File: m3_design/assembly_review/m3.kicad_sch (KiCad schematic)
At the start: 15 parts, among them J3 USB-C 2.0, U2 AP63203WU-7

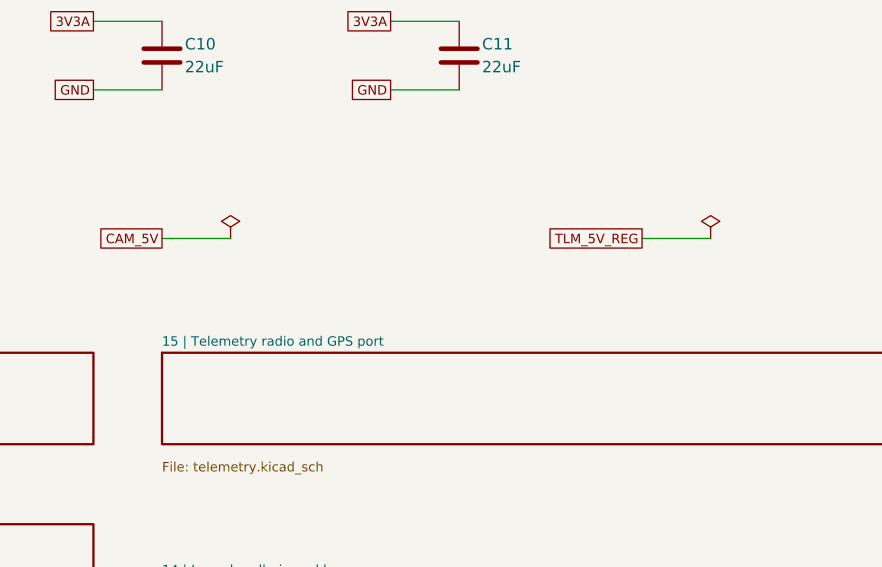
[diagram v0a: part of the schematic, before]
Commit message: M3-ASSY-R7: on-board GNSS and LoRa radio, clean-routing gate, owner-accepted deviations
R7 replaces R6's external radio/GPS harness ports with an on-board u-blox
MAX-F10S (U30, MAX-M10S drop-in) and EBYTE E22-900MM22S SX1262 radio (U31)
in an RF strip at the aft end, each with an edge-launch SMA jack (J30 GNSS,
J31 RADIO), RF ESD, an antenna-bias current limiter and DNP tuning pads.
The board grows to 46 x 118 mm (R6 copper translated +18 mm).

- Schematic, parts and footprints: r7_sch.py, r7_parts.py
- Reproducible board build from the SHA-checked R6 board: r7_build.sh
  (r7_pcb, r7_route, r7_redraw, r7_rework, r7_hygiene, r7_polish, r7_post)
- Gate: check_r7.py (RF contract), route_check.py (clean routing, M2)
  in tools/check.sh; fit_check, cost and procurement updated for R7
- Eight independent review passes with skeptic verification; pass 8 on
  this board found 0 Critical / 0 Major
- Owner accepted the deviation list on 2026-10-18 (R7_VALIDATION), with
  the 7.7 A servo-feed copper rise accepted as estimated

Board SHA-256 c872a3d30509cccf5f78b64cde48ef722ee85c7be23c4848b07ce4082a852de3.
tools/check.sh: DRC 0, unconnected 0, parity 0, ERC 0; audit, silk,
R7 contract, routing hygiene (0 failing), actuator contract and fit OK.
Before ordering: consign U4 and get JLC's forward-rail confirmation.

Co-Authored-By: Claude Opus 5.5 <noreply@anthropic.com>
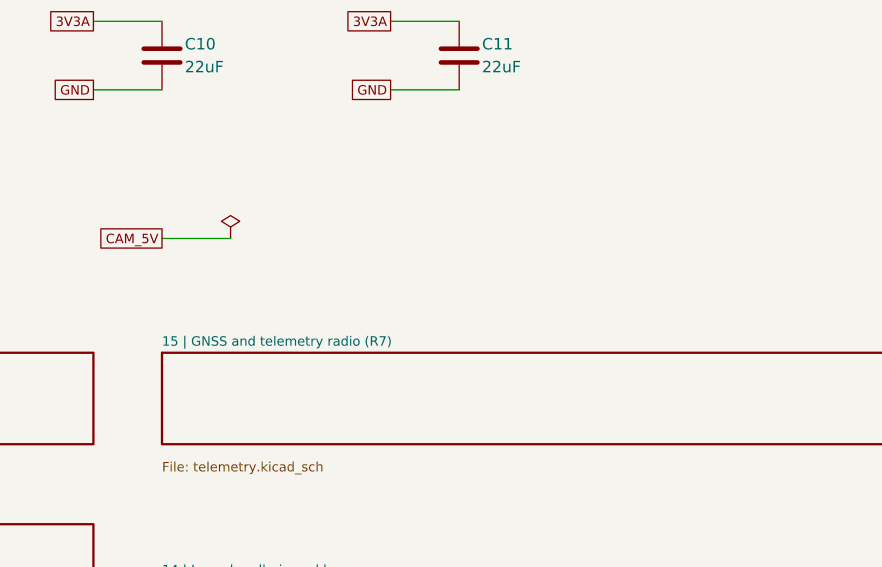
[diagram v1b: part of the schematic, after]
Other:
- sheet 15 | Telemetry radio and GPS port renamed 15 | GNSS and telemetry radio (R7)
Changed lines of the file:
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@@
 		(title "01 | USB input and regulated supplies")
 		(date "2026-09-07")
-		(rev "M3-ASSY-R6")
+		(rev "M3-ASSY-R7")
 		(company "Single-board M3 candidate; full system incomplete"))
 	(text "01 | USB input and regulated supplies"
@@
 			(justify right))
 )
-	(symbol
-		(lib_id "M3:PWR_FLAG")
-		(at 355.6 218.44 0)
-		(unit 1)
-		(in_bom no)
-		(on_board no)
-		(dnp no)
-		(property "Reference" "#FLG07"
-			(at 355.6 210.82 0)
-			(hide yes)
-			(effects
-				(font
-					(size 1.27 1.27))))
-		(property "Value" "PWR_FLAG"
-			(at 355.6 214.63 0)
-			(hide yes)
-			(effects
-				(font
-					(size 1.27 1.27))))
-		(property "Footprint" ""
-			(at 355.6 218.44 0)
-			(hide yes)
-			(effects
-				(font
-					(size 1.27 1.27))))
-		(property "Datasheet" ""
-			(at 355.6 218.44 0)
-			(hide yes)
-			(effects
-				(font
-					(size 1.27 1.27))))
-		(property "LCSC" ""
-			(at 355.6 218.44 0)
-			(hide yes)
-			(effects
-				(font
-					(size 1.27 1.27))))
-		(instances
-			(project "m3"
-				(path "/6007a7db-6a58-5660-8beb-956dea045ff8"
-					(reference "#FLG07")
-					(unit 1)))))
-	(wire
-		(pts
-			(xy 355.6 218.44)
-			(xy 347.98 218.44))
-		(stroke
-			(width 0)
-			(type default))
-)
-	(global_label "TLM_5V_REG"
-		(shape passive)
-		(at 347.98 218.44 0)
-		(effects
-			(font
-				(size 1.05 1.05))
-			(justify right))
-)
 	(sheet
 		(at 20.32 231.14)
@@
 		(fill
 			(color 0 0 0 0))
-		(property "Sheetname" "15 | Telemetry radio and GPS port"
+		(property "Sheetname" "15 | GNSS and telemetry radio (R7)"
 			(at 294.64 229.87 0)
 			(effects
